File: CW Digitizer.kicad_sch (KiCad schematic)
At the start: 28 parts, among them J1 9-20 VDC, J2 INPUT, J3 OUTPUT, U1 LM741, U2 L78L05_TO92, U3 LM567

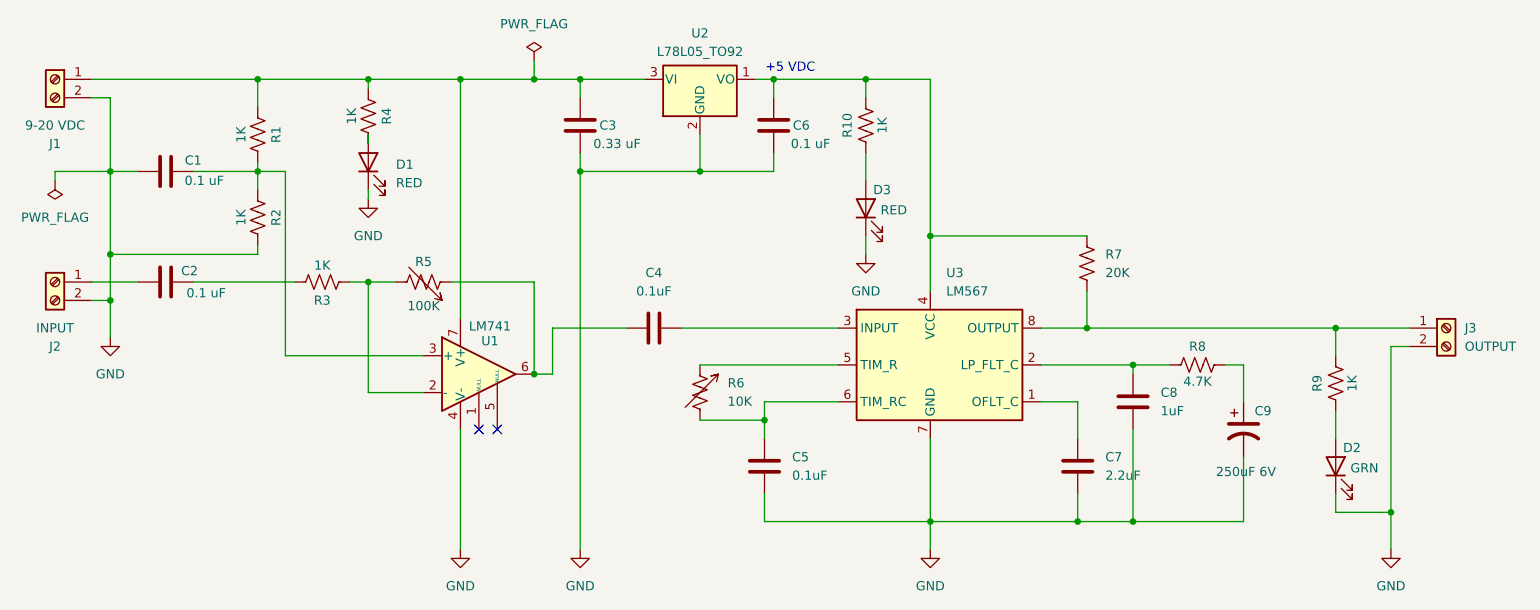
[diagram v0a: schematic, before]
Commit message: Add files via upload
Updated the schematic and PCB files to the latest version as referenced in The Communicator, Sept/Oct 2024.
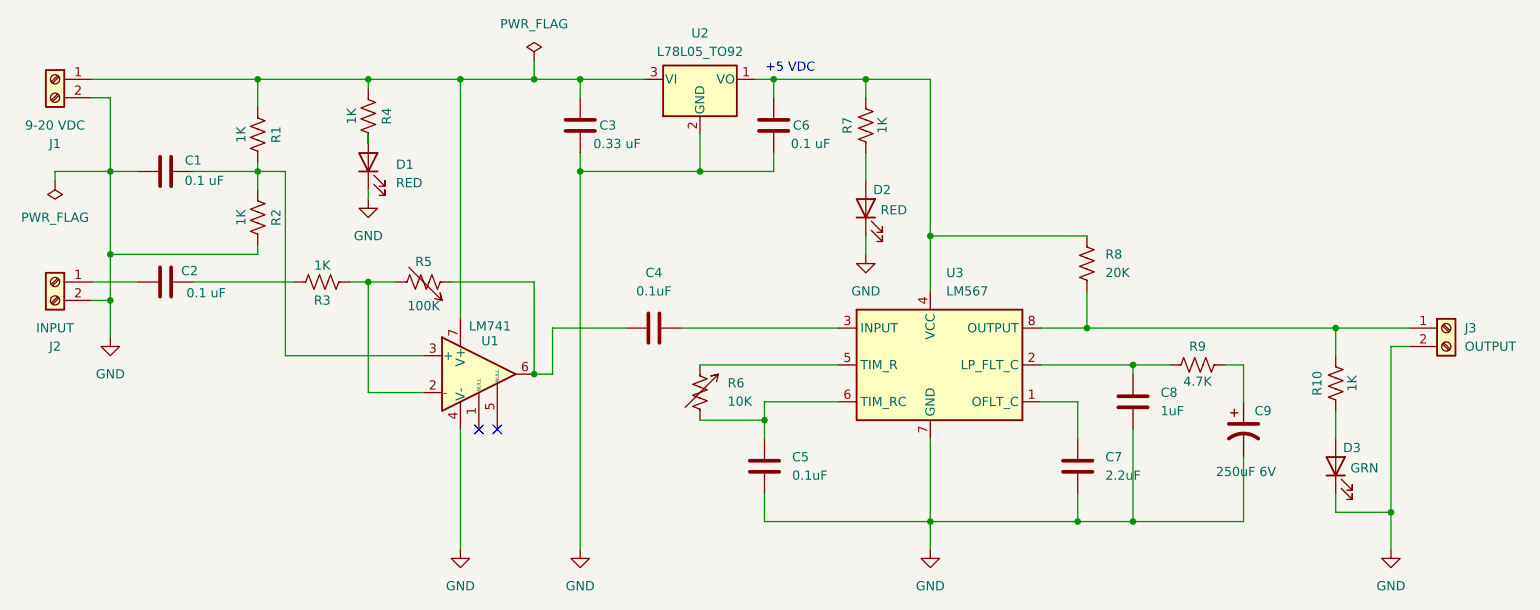
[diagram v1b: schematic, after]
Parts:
- renumbered D3 to D2, D2 to D3, R9 to R10, R10 to R7, R7 to R8, R8 to R9
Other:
- title: CW Digitizer -> Easy CW Decoder
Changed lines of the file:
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@@
 	(paper "USLetter")
 	(title_block
-		(title "CW Digitizer")
+		(title "Easy CW Decoder")
 		(date "2024-05-07")
-		(rev "1.2")
+		(rev "1.3")
 		(company "VE7ZD/KN7Q")
 	)
@@
 		(dnp no)
 		(fields_autoplaced yes)
-		(property "Reference" "#FLG02"
+		(property "Reference" "#FLG01"
 			(at 57.15 93.345 0)
 			(effects
@@
 			(project "CW Digitizer"
 				(path "/dc5f86ea-0506-419e-a8d0-e29b2a8d7f3d"
-					(reference "#FLG02")
+					(reference "#FLG01")
 					(unit 1)
 				)
@@
 		(dnp no)
 		(fields_autoplaced yes)
-		(property "Reference" "R7"
+		(property "Reference" "R8"
 			(at 201.93 101.5999 0)
 			(effects
@@
 			(project "CW Digitizer"
 				(path "/dc5f86ea-0506-419e-a8d0-e29b2a8d7f3d"
-					(reference "R7")
+					(reference "R8")
 					(unit 1)
 				)
@@
 		(on_board yes)
 		(dnp no)
-		(property "Reference" "R10"
+		(property "Reference" "R7"
 			(at 166.37 83.82 90)
 			(effects
@@
 			(project "CW Digitizer"
 				(path "/dc5f86ea-0506-419e-a8d0-e29b2a8d7f3d"
-					(reference "R10")
+					(reference "R7")
 					(unit 1)
 				)
@@
 		(on_board yes)
 		(dnp no)
-		(property "Reference" "D3"
+		(property "Reference" "D2"
 			(at 169.926 92.71 90)
 			(effects
@@
 			(project "CW Digitizer"
 				(path "/dc5f86ea-0506-419e-a8d0-e29b2a8d7f3d"
-					(reference "D3")
+					(reference "D2")
 					(unit 1)
 				)
@@
 		(on_board yes)
 		(dnp no)
-		(property "Reference" "D2"
+		(property "Reference" "D3"
 			(at 234.696 128.27 90)
 			(effects
@@
 			(project "CW Digitizer"
 				(path "/dc5f86ea-0506-419e-a8d0-e29b2a8d7f3d"
-					(reference "D2")
+					(reference "D3")
 					(unit 1)
 				)
@@
 		(on_board yes)
 		(dnp no)
-		(property "Reference" "R9"
+		(property "Reference" "R10"
 			(at 231.14 119.38 90)
 			(effects
@@
 			(project "CW Digitizer"
 				(path "/dc5f86ea-0506-419e-a8d0-e29b2a8d7f3d"
-					(reference "R9")
+					(reference "R10")
 					(unit 1)
 				)
@@
 		(dnp no)
 		(fields_autoplaced yes)
-		(property "Reference" "#FLG01"
+		(property "Reference" "#FLG02"
 			(at 123.19 73.025 0)
 			(effects
@@
 			(project "CW Digitizer"
 				(path "/dc5f86ea-0506-419e-a8d0-e29b2a8d7f3d"
-					(reference "#FLG01")
+					(reference "#FLG02")
 					(unit 1)
 				)
@@
 		(dnp no)
 		(fields_autoplaced yes)
-		(property "Reference" "#PWR06"
+		(property "Reference" "#PWR07"
 			(at 241.3 148.59 0)
 			(effects
@@
 			(project "CW Digitizer"
 				(path "/dc5f86ea-0506-419e-a8d0-e29b2a8d7f3d"
-					(reference "#PWR06")
+					(reference "#PWR07")
 					(unit 1)
 				)
@@
 		(dnp no)
 		(fields_autoplaced yes)
-		(property "Reference" "#PWR05"
+		(property "Reference" "#PWR06"
 			(at 177.8 148.59 0)
 			(effects
@@
 			(project "CW Digitizer"
 				(path "/dc5f86ea-0506-419e-a8d0-e29b2a8d7f3d"
-					(reference "#PWR05")
+					(reference "#PWR06")
 					(unit 1)
 				)
@@
 		(on_board yes)
 		(dnp no)
-		(property "Reference" "R8"
+		(property "Reference" "R9"
 			(at 214.63 114.3 90)
 			(effects
@@
 			(project "CW Digitizer"
 				(path "/dc5f86ea-0506-419e-a8d0-e29b2a8d7f3d"
-					(reference "R8")
+					(reference "R9")
 					(unit 1)
 				)
@@
 		(dnp no)
 		(fields_autoplaced yes)
-		(property "Reference" "#PWR07"
+		(property "Reference" "#PWR05"
 			(at 168.91 107.95 0)
 			(effects
@@
 			(project "CW Digitizer"
 				(path "/dc5f86ea-0506-419e-a8d0-e29b2a8d7f3d"
-					(reference "#PWR07")
+					(reference "#PWR05")
 					(unit 1)
 				)
